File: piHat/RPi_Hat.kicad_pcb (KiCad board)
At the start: 2 copper layers, 65 x 56 mm, 5 parts, among them J1 RPi_GPIO

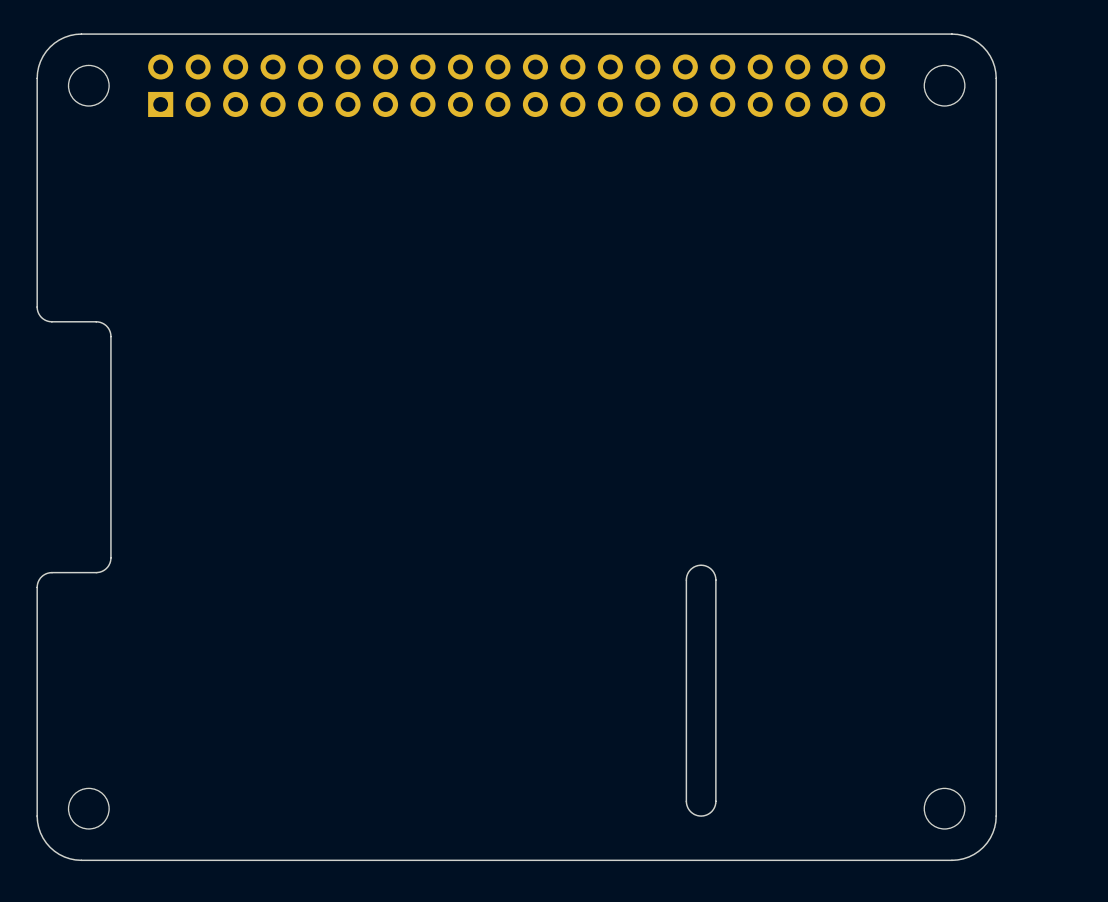
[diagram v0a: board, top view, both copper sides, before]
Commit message: add rough pcb layout
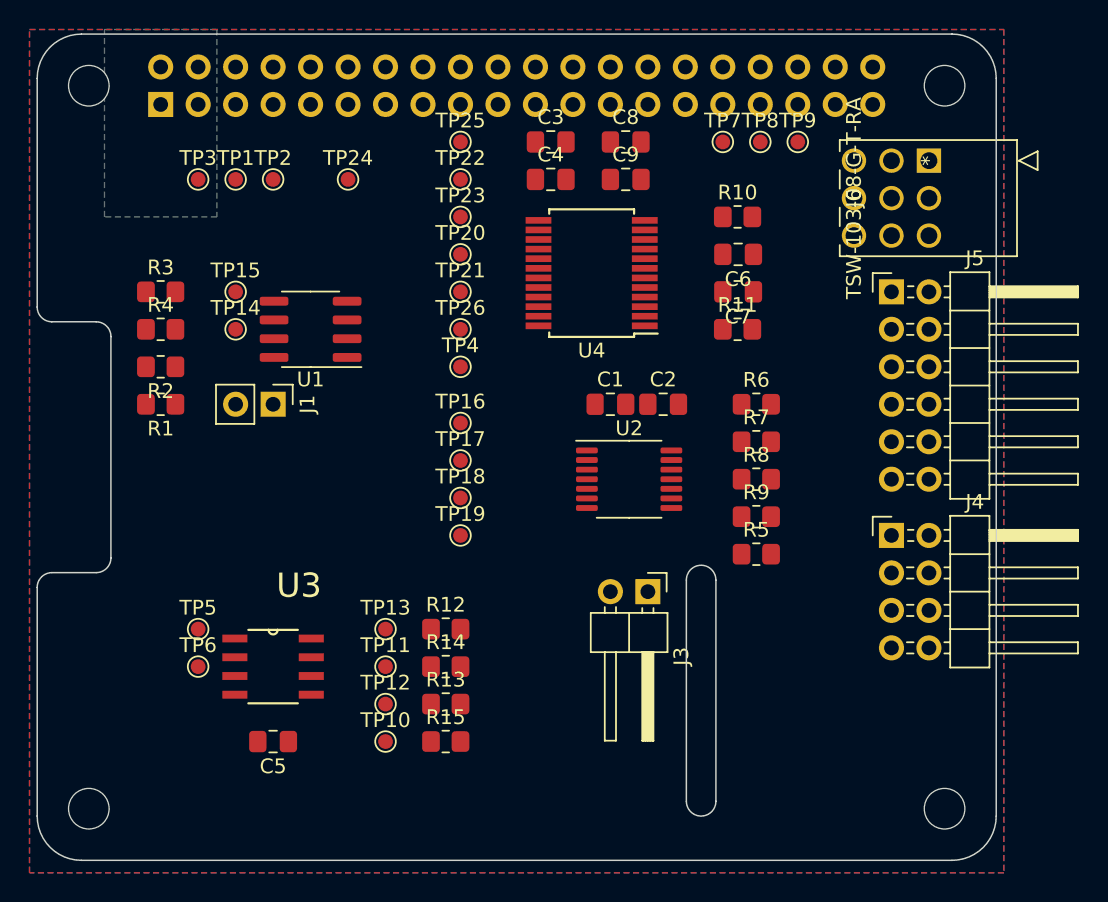
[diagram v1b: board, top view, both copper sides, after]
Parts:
- added C1: 0.1u, Capacitor_SMD:C_0805_2012Metric_Pad1.18x1.45mm_HandSolder, F.Cu at (134.6, 73.7)
- added C2: 0.1u, Capacitor_SMD:C_0805_2012Metric_Pad1.18x1.45mm_HandSolder, F.Cu at (138.2, 73.7)
- added C3: 0.1u, Capacitor_SMD:C_0805_2012Metric_Pad1.18x1.45mm_HandSolder, F.Cu at (130.6, 55.9)
- added C4: 10u, Capacitor_SMD:C_0805_2012Metric_Pad1.18x1.45mm_HandSolder, F.Cu at (130.6, 58.4)
- added C5: 0.1u, Capacitor_SMD:C_0805_2012Metric_Pad1.18x1.45mm_HandSolder, F.Cu at (111.8, 96.5)
- added C6: ?, Capacitor_SMD:C_0805_2012Metric_Pad1.18x1.45mm_HandSolder, F.Cu at (143.3, 63.5)
- added C7: ?, Capacitor_SMD:C_0805_2012Metric_Pad1.18x1.45mm_HandSolder, F.Cu at (143.3, 66.0)
- added C8: 0.1u, Capacitor_SMD:C_0805_2012Metric_Pad1.18x1.45mm_HandSolder, F.Cu at (135.7, 55.9)
- added C9: 10u, Capacitor_SMD:C_0805_2012Metric_Pad1.18x1.45mm_HandSolder, F.Cu at (135.7, 58.4)
- added J1: CONN_01X02, Connector_PinHeader_2.54mm:PinHeader_1x02_P2.54mm_Vertical, F.Cu at (111.8, 73.7)
- added J3: 12V in, Connector_PinHeader_2.54mm:PinHeader_1x02_P2.54mm_Horizontal, F.Cu at (137.2, 86.4)
- added J4: Conn_02x04_Row_Letter_First, Connector_PinHeader_2.54mm:PinHeader_2x04_P2.54mm_Horizontal, F.Cu at (153.7, 82.5)
- added J5: Conn_02x06_Row_Letter_First, Connector_PinHeader_2.54mm:PinHeader_2x06_P2.54mm_Horizontal, F.Cu at (153.7, 66.0)
- added J6: TSW-103-08-G-T-RA, piHat:TSW-103-08-G-T-RA, F.Cu at (156.2, 57.1)
- added R1: DNP, Resistor_SMD:R_0805_2012Metric_Pad1.20x1.40mm_HandSolder, F.Cu at (104.1, 73.7)
- added R10: ?, Resistor_SMD:R_0805_2012Metric_Pad1.20x1.40mm_HandSolder, F.Cu at (143.2, 61.0)
- added R11: ?, Resistor_SMD:R_0805_2012Metric_Pad1.20x1.40mm_HandSolder, F.Cu at (143.2, 68.6)
- added R12: 1.8k, Resistor_SMD:R_0805_2012Metric_Pad1.20x1.40mm_HandSolder, F.Cu at (123.5, 88.9)
- added R13: 1.8k, Resistor_SMD:R_0805_2012Metric_Pad1.20x1.40mm_HandSolder, F.Cu at (123.5, 94.0)
- added R14: 1.8k, Resistor_SMD:R_0805_2012Metric_Pad1.20x1.40mm_HandSolder, F.Cu at (123.5, 91.4)
- added R15: 1.8k, Resistor_SMD:R_0805_2012Metric_Pad1.20x1.40mm_HandSolder, F.Cu at (123.5, 96.5)
- added R2: 10K, Resistor_SMD:R_0805_2012Metric_Pad1.20x1.40mm_HandSolder, F.Cu at (104.1, 71.1)
- added R3: 3.9K, Resistor_SMD:R_0805_2012Metric_Pad1.20x1.40mm_HandSolder, F.Cu at (104.1, 66.0)
- added R4: 3.9K, Resistor_SMD:R_0805_2012Metric_Pad1.20x1.40mm_HandSolder, F.Cu at (104.1, 68.6)
- added R5: 3.8k, Resistor_SMD:R_0805_2012Metric_Pad1.20x1.40mm_HandSolder, F.Cu at (144.5, 83.8)
- added R6: 3.8k, Resistor_SMD:R_0805_2012Metric_Pad1.20x1.40mm_HandSolder, F.Cu at (144.5, 73.7)
- added R7: 3.8k, Resistor_SMD:R_0805_2012Metric_Pad1.20x1.40mm_HandSolder, F.Cu at (144.5, 76.2)
- added R8: 3.8k, Resistor_SMD:R_0805_2012Metric_Pad1.20x1.40mm_HandSolder, F.Cu at (144.5, 78.7)
- added R9: 3.8k, Resistor_SMD:R_0805_2012Metric_Pad1.20x1.40mm_HandSolder, F.Cu at (144.5, 81.3)
- added TP1: DIS_EL_TP, TestPoint:TestPoint_Pad_D1.0mm, F.Cu at (109.2, 58.4)
- added TP10: DIS_EL_TP, TestPoint:TestPoint_Pad_D1.0mm, F.Cu at (119.4, 96.5)
- added TP11: DIS_EL_TP, TestPoint:TestPoint_Pad_D1.0mm, F.Cu at (119.4, 91.4)
- added TP12: DIS_EL_TP, TestPoint:TestPoint_Pad_D1.0mm, F.Cu at (119.4, 94.0)
- added TP13: DIS_EL_TP, TestPoint:TestPoint_Pad_D1.0mm, F.Cu at (119.4, 88.9)
- added TP14: DIS_EL_TP, TestPoint:TestPoint_Pad_D1.0mm, F.Cu at (109.2, 68.6)
- added TP15: DIS_EL_TP, TestPoint:TestPoint_Pad_D1.0mm, F.Cu at (109.2, 66.0)
- added TP16: DIS_EL_TP, TestPoint:TestPoint_Pad_D1.0mm, F.Cu at (124.5, 74.9)
- added TP17: DIS_EL_TP, TestPoint:TestPoint_Pad_D1.0mm, F.Cu at (124.5, 77.5)
- added TP18: DIS_EL_TP, TestPoint:TestPoint_Pad_D1.0mm, F.Cu at (124.5, 80.0)
- added TP19: DIS_EL_TP, TestPoint:TestPoint_Pad_D1.0mm, F.Cu at (124.5, 82.5)
- added TP2: DIS_EL_TP, TestPoint:TestPoint_Pad_D1.0mm, F.Cu at (111.8, 58.4)
- added TP20: DIS_EL_TP, TestPoint:TestPoint_Pad_D1.0mm, F.Cu at (124.5, 63.5)
- added TP21: DIS_EL_TP, TestPoint:TestPoint_Pad_D1.0mm, F.Cu at (124.5, 66.0)
- added TP22: DIS_EL_TP, TestPoint:TestPoint_Pad_D1.0mm, F.Cu at (124.5, 58.4)
- added TP23: DIS_EL_TP, TestPoint:TestPoint_Pad_D1.0mm, F.Cu at (124.5, 61.0)
- added TP24: DIS_EL_TP, TestPoint:TestPoint_Pad_D1.0mm, F.Cu at (116.8, 58.4)
- added TP25: DIS_EL_TP, TestPoint:TestPoint_Pad_D1.0mm, F.Cu at (124.5, 55.9)
- added TP26: DIS_EL_TP, TestPoint:TestPoint_Pad_D1.0mm, F.Cu at (124.5, 68.6)
- added TP3: DIS_EL_TP, TestPoint:TestPoint_Pad_D1.0mm, F.Cu at (106.7, 58.4)
- added TP4: DIS_EL_TP, TestPoint:TestPoint_Pad_D1.0mm, F.Cu at (124.5, 71.1)
- added TP5: DIS_EL_TP, TestPoint:TestPoint_Pad_D1.0mm, F.Cu at (106.7, 88.9)
- added TP6: DIS_EL_TP, TestPoint:TestPoint_Pad_D1.0mm, F.Cu at (106.7, 91.4)
- added TP7: DIS_EL_TP, TestPoint:TestPoint_Pad_D1.0mm, F.Cu at (142.2, 55.9)
- added TP8: DIS_EL_TP, TestPoint:TestPoint_Pad_D1.0mm, F.Cu at (144.8, 55.9)
- added TP9: DIS_EL_TP, TestPoint:TestPoint_Pad_D1.0mm, F.Cu at (147.3, 55.9)
- added U1: CAT24C32, Package_SO:SOIC-8_3.9x4.9mm_P1.27mm, F.Cu at (114.3, 68.6)
- added U2: TXB0104PW, Package_SO:TSSOP-14_4.4x5mm_P0.65mm, F.Cu at (135.9, 78.7)
- added U3: PCA9540BD,118, SOIC127P600X175-8N, F.Cu at (111.8, 91.4)
- added U4: TB6612FNG, Package_SO:SSOP-24_5.3x8.2mm_P0.65mm, F.Cu at (133.3, 64.8)
- H1, H2, H3, H4: value MountingHole -> 3mm_Mounting_Hole
- renumbered J1 to J2
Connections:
- J2 pad 1: Net-(J1-Pad1) -> +3V3
- J2 pad 10: Net-(J1-Pad10) -> (no net)
- J2 pad 11: Net-(J1-Pad11) -> /SW0
- J2 pad 12: Net-(J1-Pad12) -> (no net)
- J2 pad 13: Net-(J1-Pad13) -> /SW1
- J2 pad 14: Net-(J1-Pad14) -> GND
- J2 pad 15: Net-(J1-Pad15) -> /SW2
- J2 pad 16: Net-(J1-Pad16) -> /MOTOR_STBY
- J2 pad 17: Net-(J1-Pad17) -> +3V3
- J2 pad 18: Net-(J1-Pad18) -> /MOTOR_AIN1
- J2 pad 19: Net-(J1-Pad19) -> (no net)
- J2 pad 2: Net-(J1-Pad2) -> +5V
- J2 pad 20: Net-(J1-Pad20) -> GND
- J2 pad 21: Net-(J1-Pad21) -> (no net)
- J2 pad 22: Net-(J1-Pad22) -> /MOTOR_AIN2
- J2 pad 23: Net-(J1-Pad23) -> (no net)
- J2 pad 24: Net-(J1-Pad24) -> /MOTOR_BIN1
- J2 pad 25: Net-(J1-Pad25) -> GND
- J2 pad 26: Net-(J1-Pad26) -> /MOTOR_BIN2
- J2 pad 27: Net-(J1-Pad27) -> /ID_SD_EEPROM
- J2 pad 28: Net-(J1-Pad28) -> /ID_SC_EEPROM
- J2 pad 29: Net-(J1-Pad29) -> /ENCODER0_M0
- J2 pad 3: Net-(J1-Pad3) -> /SDA
- J2 pad 30: Net-(J1-Pad30) -> GND
- J2 pad 31: Net-(J1-Pad31) -> /ENCODER1_M0
- J2 pad 32: Net-(J1-Pad32) -> /MOTOR_PWM0
- J2 pad 33: Net-(J1-Pad33) -> /MOTOR_PWM1
- J2 pad 34: Net-(J1-Pad34) -> GND
- J2 pad 35: Net-(J1-Pad35) -> (no net)
- J2 pad 36: Net-(J1-Pad36) -> /ENCODER1_M1
- J2 pad 37: Net-(J1-Pad37) -> /ENCODER0_M1
- J2 pad 38: Net-(J1-Pad38) -> (no net)
- J2 pad 39: Net-(J1-Pad39) -> GND
- J2 pad 4: Net-(J1-Pad4) -> +5V
- J2 pad 40: Net-(J1-Pad40) -> (no net)
- J2 pad 5: Net-(J1-Pad5) -> /SCL
- J2 pad 6: Net-(J1-Pad6) -> GND
- J2 pad 7: Net-(J1-Pad7) -> (no net)
- J2 pad 8: Net-(J1-Pad8) -> (no net)
- J2 pad 9: Net-(J1-Pad9) -> GND
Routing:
- added copper zone on B.Cu, net +5V
- added copper zone on B.Cu, net GND
- added copper zone on F.Cu, net GND
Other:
- net class 5V added: clearance 0, trace_width 0.25, via_dia 0.6, via_drill 0.4

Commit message: finalize PCB layout
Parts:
- moved TP19 32.6 mm to (145.8, 57.9)
- moved TP18 30.8 mm to (147.3, 59.4)
- moved TP17 26.4 mm to (143.3, 58.9)
- moved TP16 24.4 mm to (139.7, 55.9)
- moved TP26 22.1 mm to (142.2, 55.4)
- moved TP25 18.8 mm to (142.2, 62.0)
- moved R5 15.8 mm to (133.6, 72.4), turned to 180 degrees
- moved TP21 13.8 mm to (137.7, 62.0)
- moved C3 12.8 mm to (133.6, 68.3), turned to 180 degrees
- moved C4 12.3 mm to (133.6, 70.4), turned to 180 degrees
- moved C9 12.3 mm to (129.5, 69.1)
- moved C8 12.3 mm to (129.6, 66.5)
- moved TP6 11.2 mm to (112.3, 81.8)
- moved TP22 10.3 mm to (134.6, 59.9)
- moved TP8 10.2 mm to (134.6, 55.4)
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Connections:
- U4 pad 1: /Motor1_Out1 -> /Motor1_Out2
- U4 pad 2: /Motor1_Out1 -> /Motor1_Out2
- U4 pad 5: /Motor1_Out2 -> /Motor1_Out1
- U4 pad 6: /Motor1_Out2 -> /Motor1_Out1
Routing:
- net GND: track 0.00 -> 143.8 mm, vias 0 -> 15
- net +5V: track 0.00 -> 123.3 mm, vias 0 -> 5
- net +3V3: track 0.00 -> 105.6 mm, vias 0 -> 2
- net /SDA_ME0: track 0.00 -> 59.7 mm, vias 0 -> 1
- net /SCL_ME1: track 0.00 -> 58.1 mm, vias 0 -> 2
- net /SCL_ME0: track 0.00 -> 57.9 mm, vias 0 -> 4
- net /SDA_ME1: track 0.00 -> 54.9 mm, vias 0 -> 2
- net /ID_SC_EEPROM: track 0.00 -> 51.4 mm, vias 0 -> 5
- net /ID_SD_EEPROM: track 0.00 -> 51.3 mm, vias 0 -> 4
- net /SDA: track 0.00 -> 50.4 mm, vias 0 -> 1
- net /SCL: track 0.00 -> 44.4 mm, vias 0 -> 1
- net +12V: track 0.00 -> 41.6 mm, vias 0 -> 4
- net /SW0: track 0.00 -> 40.4 mm, vias 0 -> 2
- net /SW2: track 0.00 -> 40.4 mm, vias 0 -> 2
- net /ENCODER1_M1: track 0.00 -> 37.7 mm, vias 0 -> 2
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- added copper zone on F.Cu, net +12V
- added copper zone on F.Cu, net +3V3
- added copper zone on F.Cu, net /Motor0_Out1
- added copper zone on F.Cu, net /Motor0_Out2
- added copper zone on B.Cu, net /Motor1_Out1
- added copper zone on F.Cu, net /Motor1_Out1
- added copper zone on B.Cu, net /Motor1_Out2
- added copper zone on F.Cu, net /Motor1_Out2
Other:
- net class 5V removed
- net class High Current added: clearance 0.2, trace_width 0.762, via_dia 0.6, via_drill 0.4
- net class Power added: clearance 0.2, trace_width 0.508, via_dia 0.6, via_drill 0.4
